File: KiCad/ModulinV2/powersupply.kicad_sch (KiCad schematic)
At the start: 47 parts, among them IC36 NCP5500DADJR2G, IC37 REF195ESZ-REEL, IC38 LM2576S-12_NOPB, IC39 LM2576S-12_NOPB, IC40 NCP5500DADJR2G, IC41 REF196GSZ-REEL, IC42 L7812CD2T-TR, IC43 L7812CD2T-TR, J9 PJ-002B, Q3 DMP610DL-7

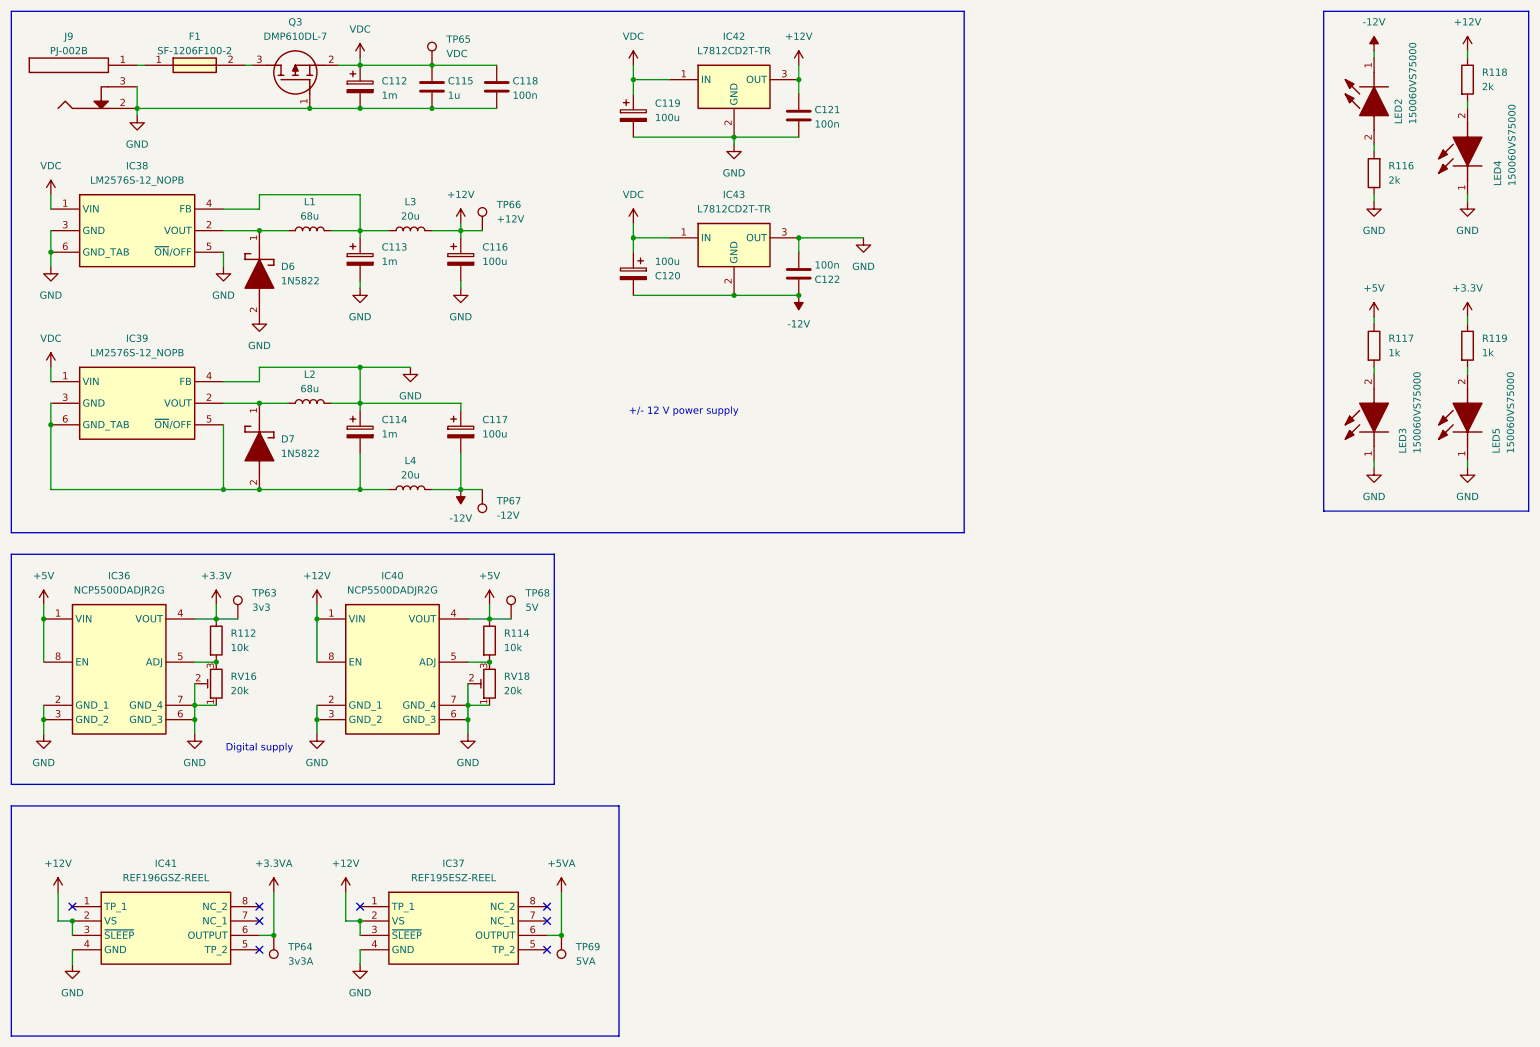
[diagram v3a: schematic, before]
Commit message: Finished Schematic, started on PCB
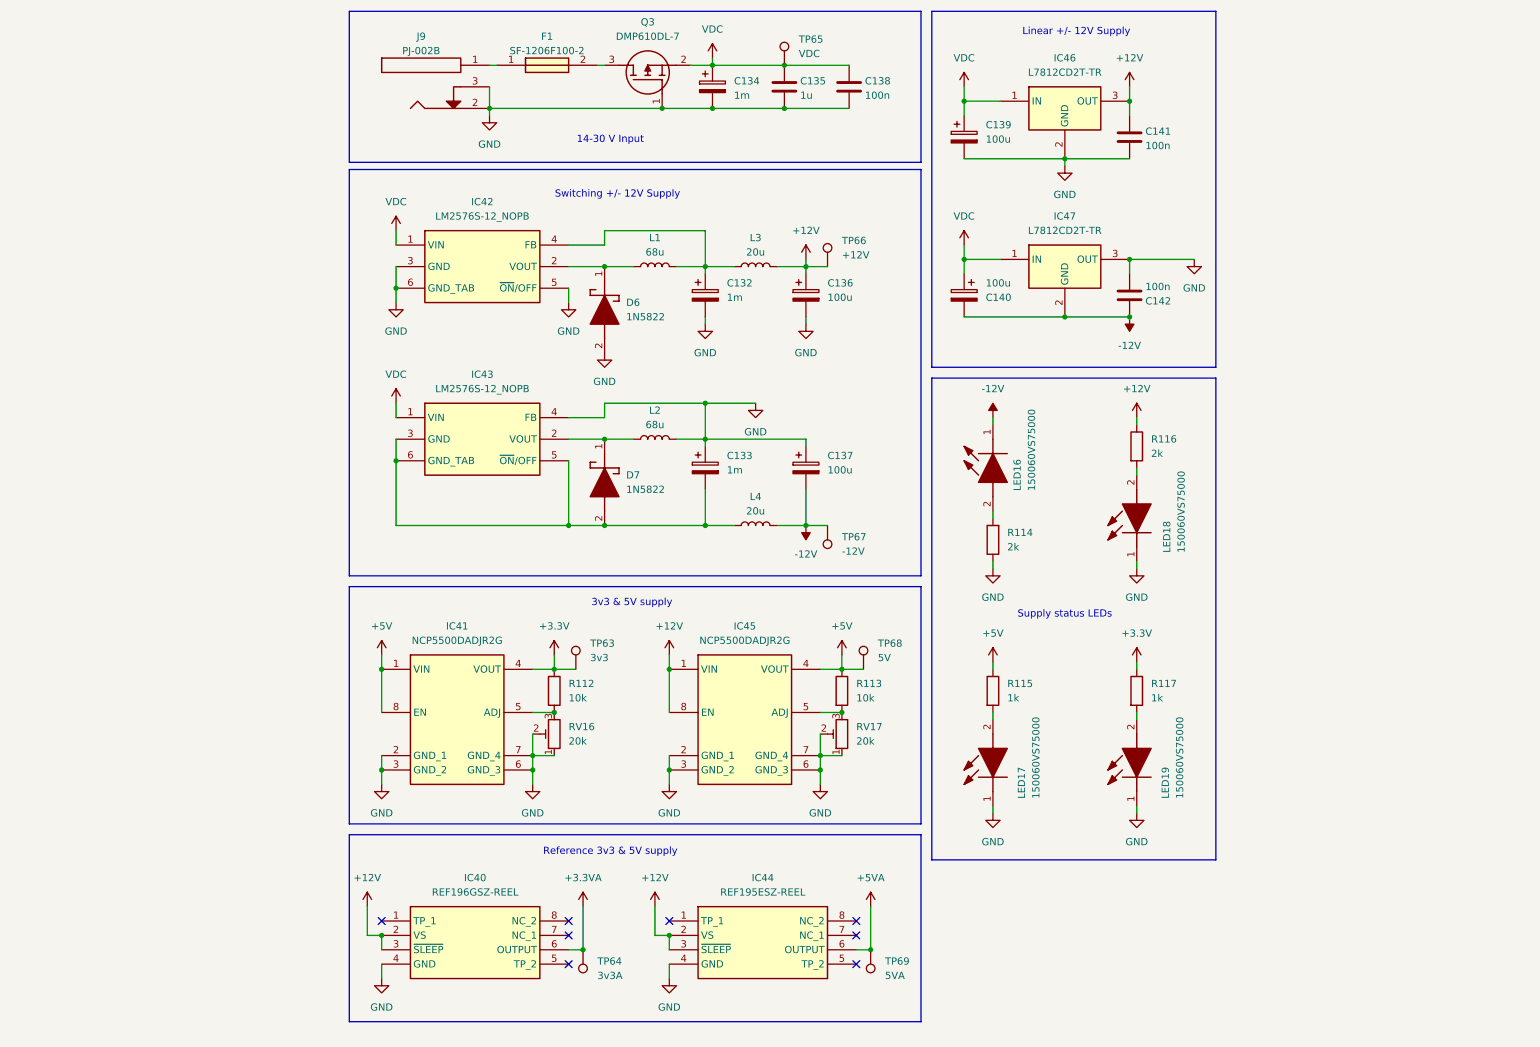
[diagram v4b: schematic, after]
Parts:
- R112: footprint (none) -> Resistor_SMD:R_0603_1608Metric_Pad0.98x0.95mm_HandSolder
- R113: renamed from R114; footprint (none) -> Resistor_SMD:R_0603_1608Metric_Pad0.98x0.95mm_HandSolder
- R114: renamed from R116; footprint (none) -> Resistor_SMD:R_0603_1608Metric_Pad0.98x0.95mm_HandSolder
- R115: renamed from R117; footprint (none) -> Resistor_SMD:R_0603_1608Metric_Pad0.98x0.95mm_HandSolder
- R116: renamed from R118; footprint (none) -> Resistor_SMD:R_0603_1608Metric_Pad0.98x0.95mm_HandSolder
- R117: renamed from R119; footprint (none) -> Resistor_SMD:R_0603_1608Metric_Pad0.98x0.95mm_HandSolder
- renumbered C113 to C132, C114 to C133, C112 to C134, C115 to C135, C116 to C136, C117 to C137, C118 to C138, C119 to C139, C120 to C140, C121 to C141, C122 to C142, IC41 to IC40, IC36 to IC41, IC38 to IC42, IC39 to IC43, IC37 to IC44, IC40 to IC45, IC42 to IC46, IC43 to IC47, LED2 to LED16, LED3 to LED17, LED4 to LED18, LED5 to LED19, RV18 to RV17
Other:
- note added: "14-30 V Input"
- note added: "3v3 & 5V supply"
- note added: "Linear +/- 12V Supply"
- note added: "Reference 3v3 & 5V supply"
- note added: "Supply status LEDs"
- note added: "Switching +/- 12V Supply"
- note removed: "+/- 12 V power supply"
- note removed: "Digital supply"
- moved on the sheet: C132, C133, C134, C135, C136, C137, C138, C139, C140, C141, C142, D6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

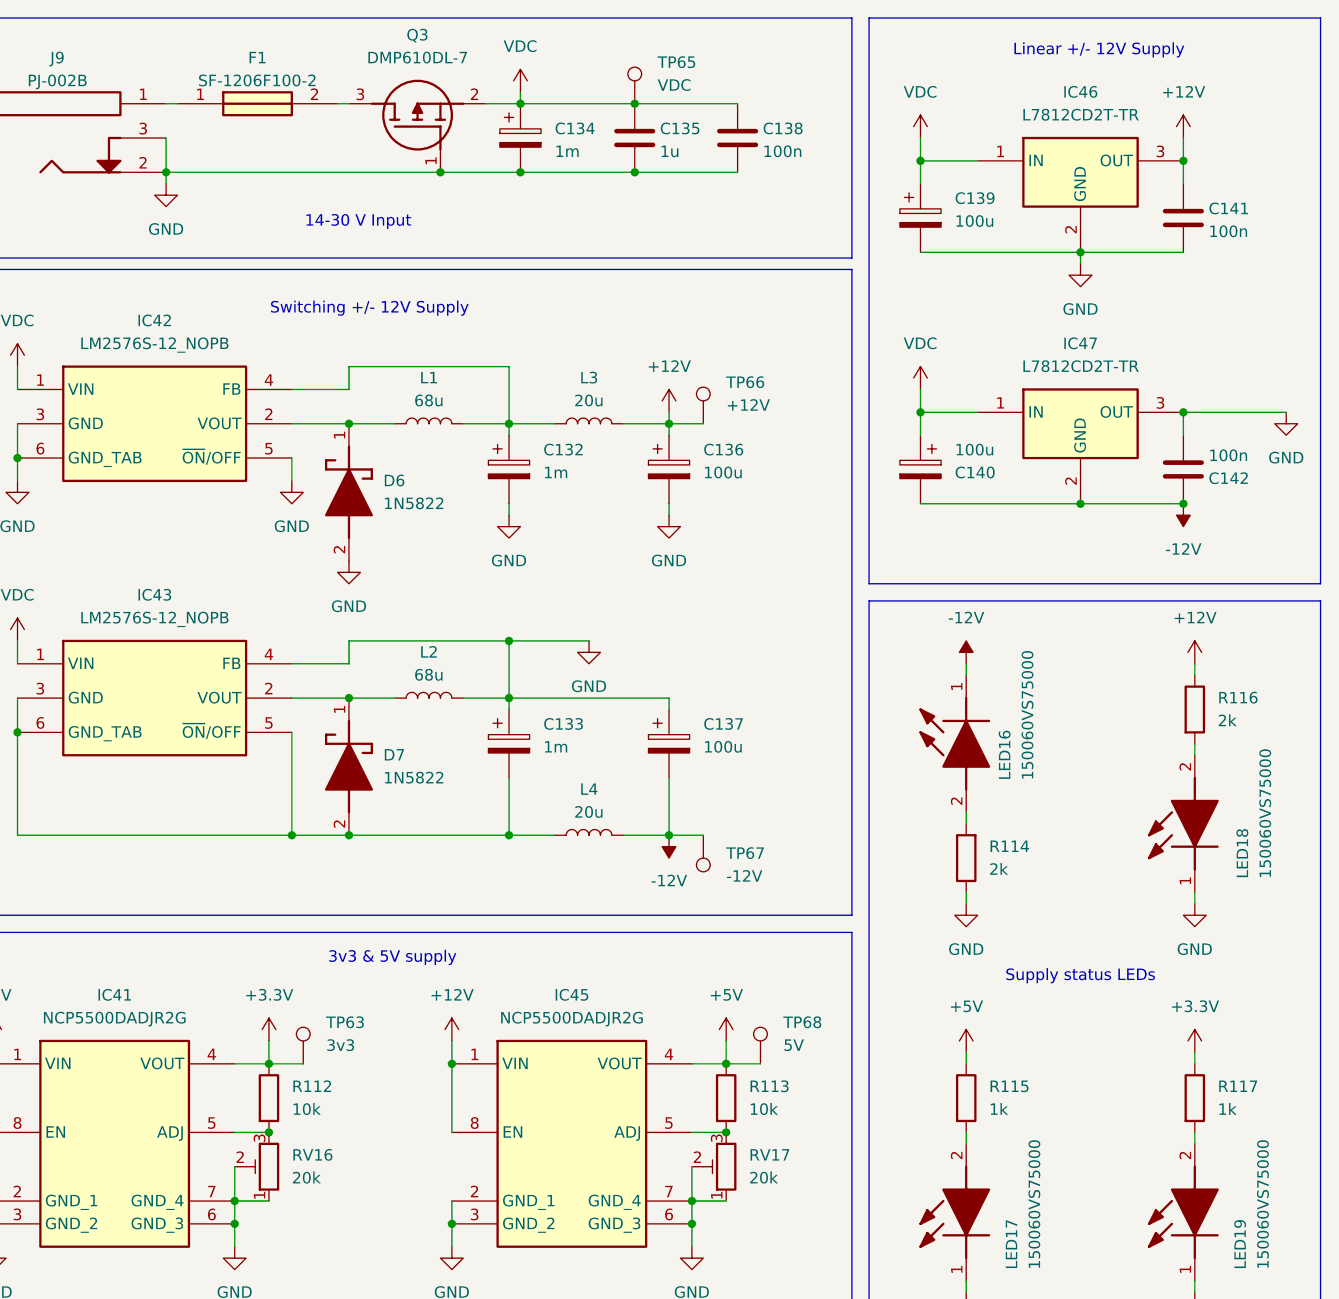
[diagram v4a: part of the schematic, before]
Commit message: Started designing the power supply layout and grouped components by the type of circuit
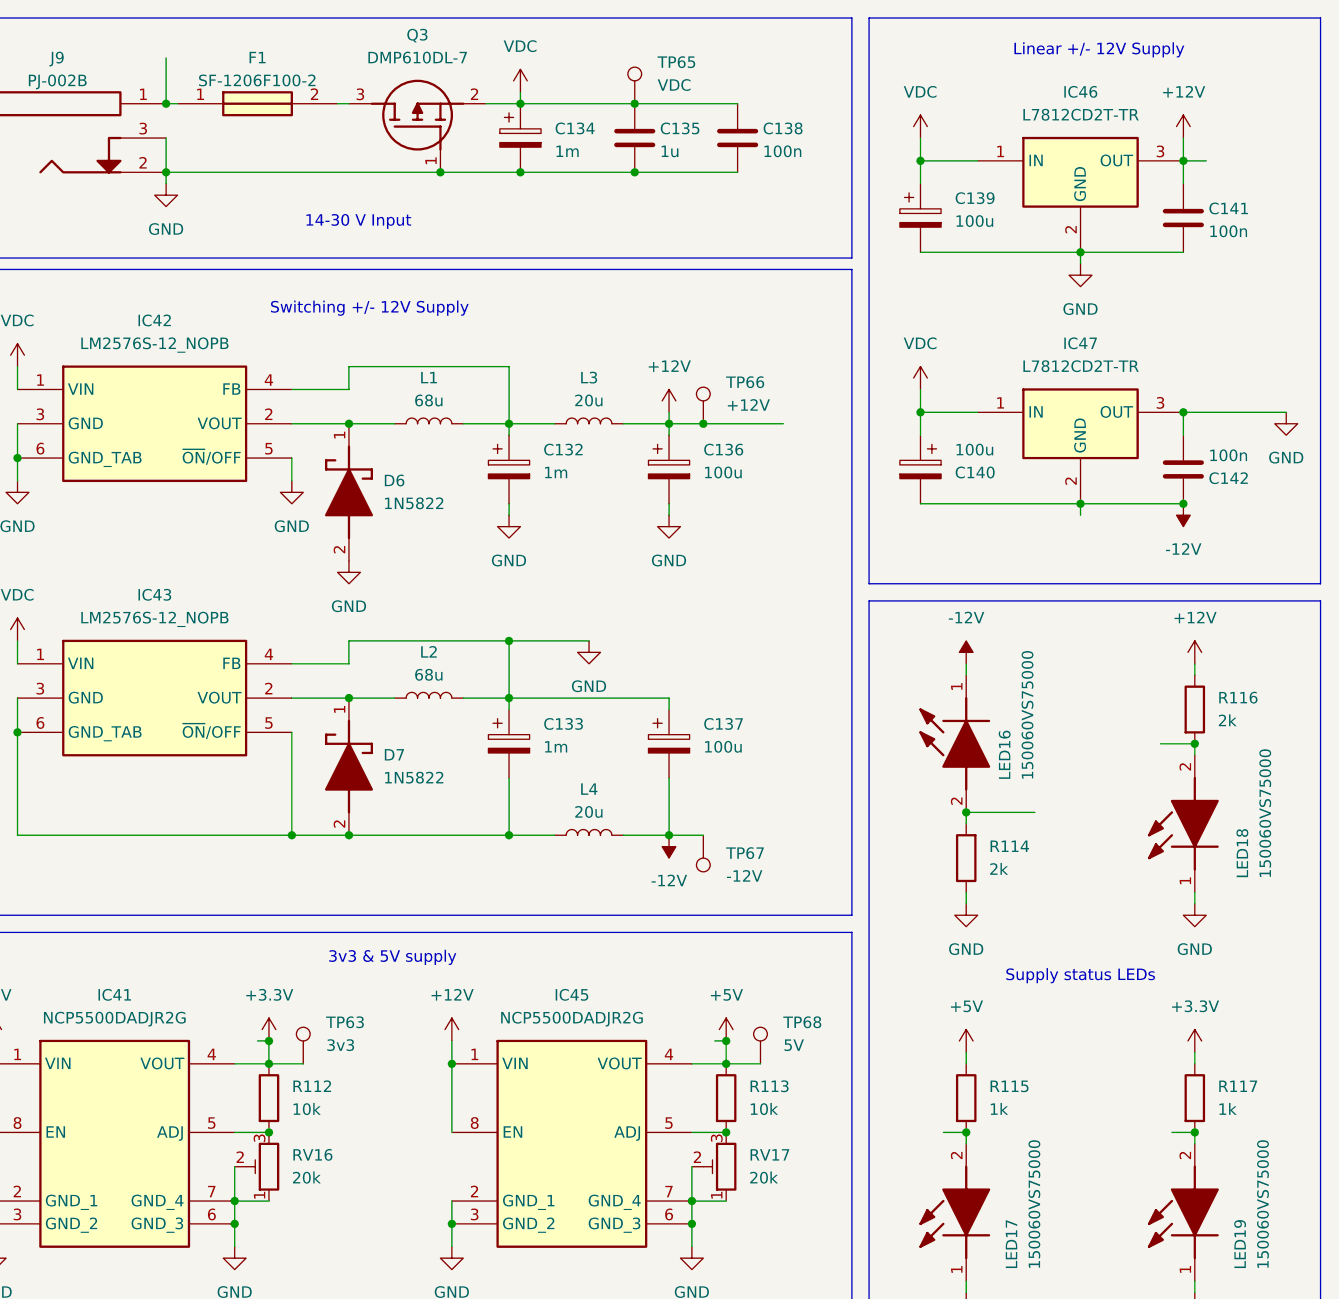
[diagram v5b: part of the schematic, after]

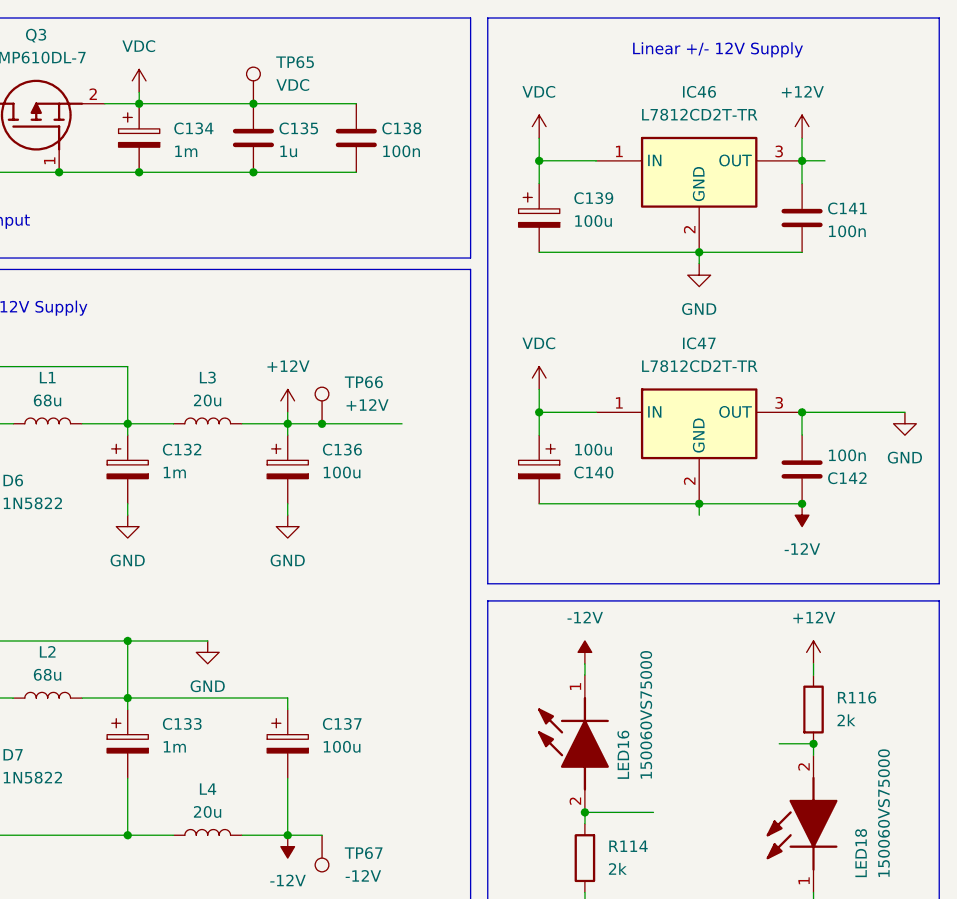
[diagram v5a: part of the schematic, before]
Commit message: Layed out Interface and PWR components and started with MCU layout
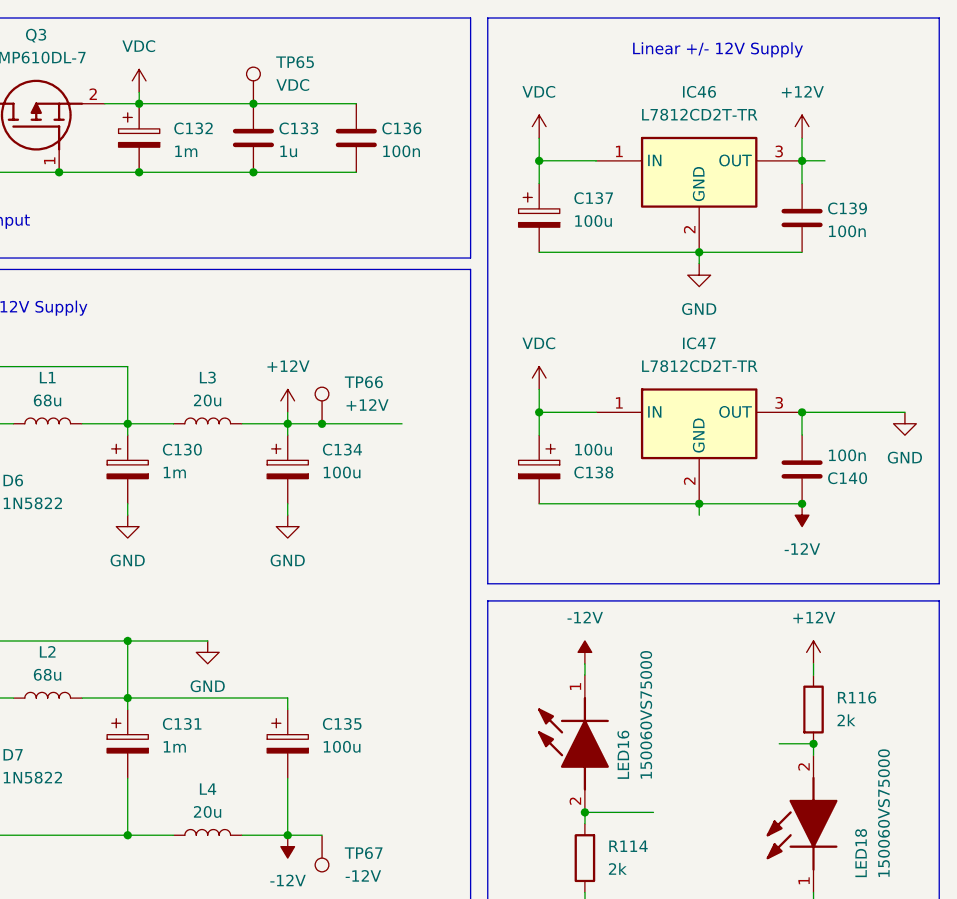
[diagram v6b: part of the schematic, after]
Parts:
- renumbered C132 to C130, C133 to C131, C134 to C132, C135 to C133, C136 to C134, C137 to C135, C138 to C136, C139 to C137, C140 to C138, C141 to C139, C142 to C140
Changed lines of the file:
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@@
 		(dnp no)
 		(fields_autoplaced yes)
-		(property "Reference" "C140"
+		(property "Reference" "C138"
 			(at 186.69 65.1511 0)
 			(effects
@@
 			(project "ModulinV2"
 				(path "/c6b34a57-3941-4b56-8b80-1848c7f41082/f36bc0c9-50e7-404a-b5bb-5b2e43f62359"
-					(reference "C140")
+					(reference "C138")
 					(unit 1)
 				)
@@
 		(on_board yes)
 		(dnp no)
-		(property "Reference" "C142"
+		(property "Reference" "C140"
 			(at 214.884 65.786 0)
 			(effects
@@
 			(project "ModulinV2"
 				(path "/c6b34a57-3941-4b56-8b80-1848c7f41082/f36bc0c9-50e7-404a-b5bb-5b2e43f62359"
-					(reference "C142")
+					(reference "C140")
 					(unit 1)
 				)
@@
 		(on_board yes)
 		(dnp no)
-		(property "Reference" "C138"
+		(property "Reference" "C136"
 			(at 165.354 26.924 0)
 			(effects
@@
 			(project "ModulinV2"
 				(path "/c6b34a57-3941-4b56-8b80-1848c7f41082/f36bc0c9-50e7-404a-b5bb-5b2e43f62359"
-					(reference "C138")
+					(reference "C136")
 					(unit 1)
 				)
@@
 		(on_board yes)
 		(dnp no)
-		(property "Reference" "C134"
+		(property "Reference" "C132"
 			(at 142.24 26.924 0)
 			(effects
@@
 			(project ""
 				(path "/c6b34a57-3941-4b56-8b80-1848c7f41082/f36bc0c9-50e7-404a-b5bb-5b2e43f62359"
-					(reference "C134")
+					(reference "C132")
 					(unit 1)
 				)
@@
 		(dnp no)
 		(fields_autoplaced yes)
-		(property "Reference" "C136"
+		(property "Reference" "C134"
 			(at 158.75 62.6109 0)
 			(effects
@@
 			(project "ModulinV2"
 				(path "/c6b34a57-3941-4b56-8b80-1848c7f41082/f36bc0c9-50e7-404a-b5bb-5b2e43f62359"
-					(reference "C136")
+					(reference "C134")
 					(unit 1)
 				)
@@
 		(on_board yes)
 		(dnp no)
-		(property "Reference" "C141"
+		(property "Reference" "C139"
 			(at 214.884 35.814 0)
 			(effects
@@
 			(project "ModulinV2"
 				(path "/c6b34a57-3941-4b56-8b80-1848c7f41082/f36bc0c9-50e7-404a-b5bb-5b2e43f62359"
-					(reference "C141")
+					(reference "C139")
 					(unit 1)
 				)
@@
 		(on_board yes)
 		(dnp no)
-		(property "Reference" "C135"
+		(property "Reference" "C133"
 			(at 153.924 26.924 0)
 			(effects
@@
 			(project "ModulinV2"
 				(path "/c6b34a57-3941-4b56-8b80-1848c7f41082/f36bc0c9-50e7-404a-b5bb-5b2e43f62359"
-					(reference "C135")
+					(reference "C133")
 					(unit 1)
 				)
@@
 		(dnp no)
 		(fields_autoplaced yes)
-		(property "Reference" "C133"
+		(property "Reference" "C131"
 			(at 140.97 93.0909 0)
 			(effects
@@
 			(project "ModulinV2"
 				(path "/c6b34a57-3941-4b56-8b80-1848c7f41082/f36bc0c9-50e7-404a-b5bb-5b2e43f62359"
-					(reference "C133")
+					(reference "C131")
 					(unit 1)
 				)
@@
 		(dnp no)
 		(fields_autoplaced yes)
-		(property "Reference" "C137"
+		(property "Reference" "C135"
 			(at 158.75 93.0909 0)
 			(effects
@@
 			(project "ModulinV2"
 				(path "/c6b34a57-3941-4b56-8b80-1848c7f41082/f36bc0c9-50e7-404a-b5bb-5b2e43f62359"
-					(reference "C137")
+					(reference "C135")
 					(unit 1)
 				)
@@
 		(dnp no)
 		(fields_autoplaced yes)
-		(property "Reference" "C132"
+		(property "Reference" "C130"
 			(at 140.97 62.6109 0)
 			(effects
@@
 			(project "ModulinV2"
 				(path "/c6b34a57-3941-4b56-8b80-1848c7f41082/f36bc0c9-50e7-404a-b5bb-5b2e43f62359"
-					(reference "C132")
+					(reference "C130")
 					(unit 1)
 				)
@@
 		(dnp no)
 		(fields_autoplaced yes)
-		(property "Reference" "C139"
+		(property "Reference" "C137"
 			(at 186.69 34.6709 0)
 			(effects
@@
 			(project "ModulinV2"
 				(path "/c6b34a57-3941-4b56-8b80-1848c7f41082/f36bc0c9-50e7-404a-b5bb-5b2e43f62359"
-					(reference "C139")
+					(reference "C137")
 					(unit 1)
 				)
